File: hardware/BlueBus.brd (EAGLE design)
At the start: 90 x 55 mm, 77 parts, among them J1 USB, Y1 32.768kHz

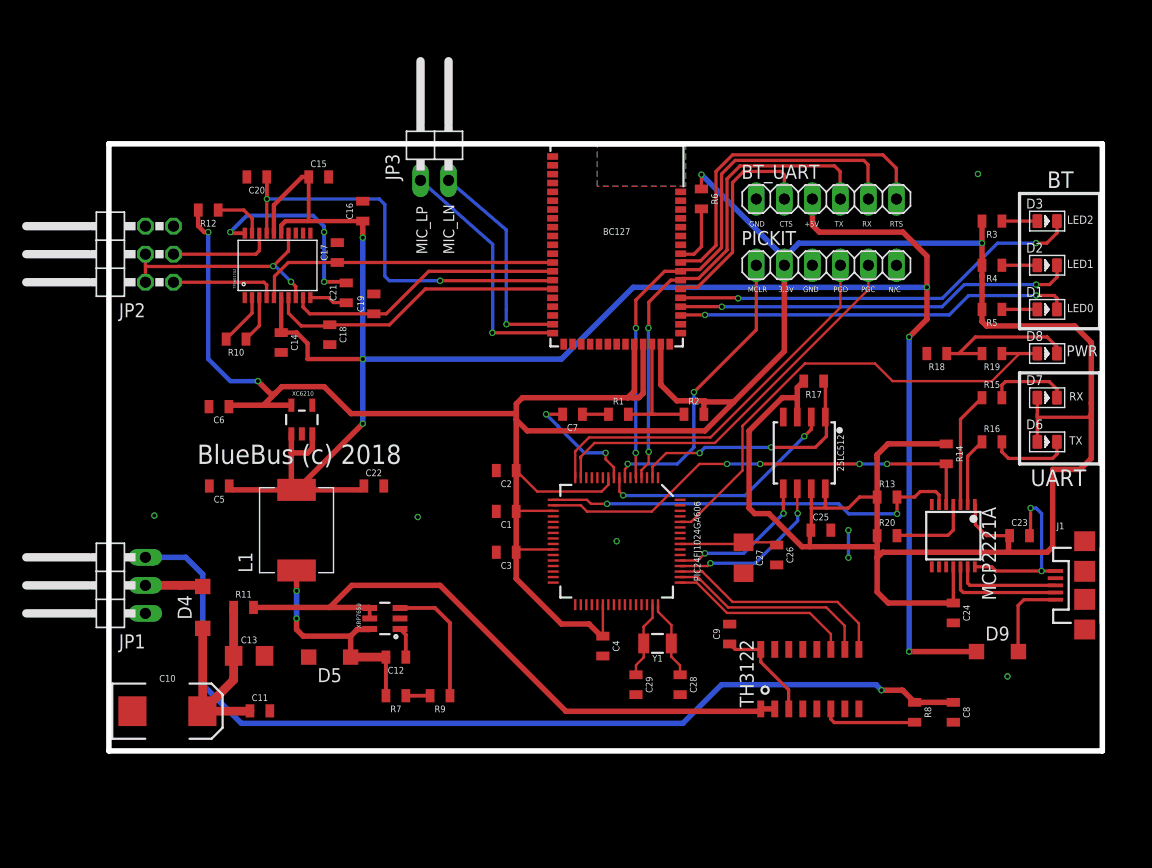
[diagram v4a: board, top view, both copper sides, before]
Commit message: [ADD] hardware: BlueBus v4 Board Changes * Remove BC127 LEDs * Enlarge all IC pads to make SMD assembly easier * Rewire 3.3v Rail into a star topology to do away with potential issues from dasiy chaining * Rewire portions of the 5V rail * Rewire MIC_IN Signals to make use of stereo audio * Tighten up similar signals for better board routing * Enlarge all vias to 0.51mm * Elarge 5v rail to 0.55mm * Tent all vias for a nicer silkscreen * Update silkscreen positioning * Remove wires from under TPA6013 since it contains a thermal pad
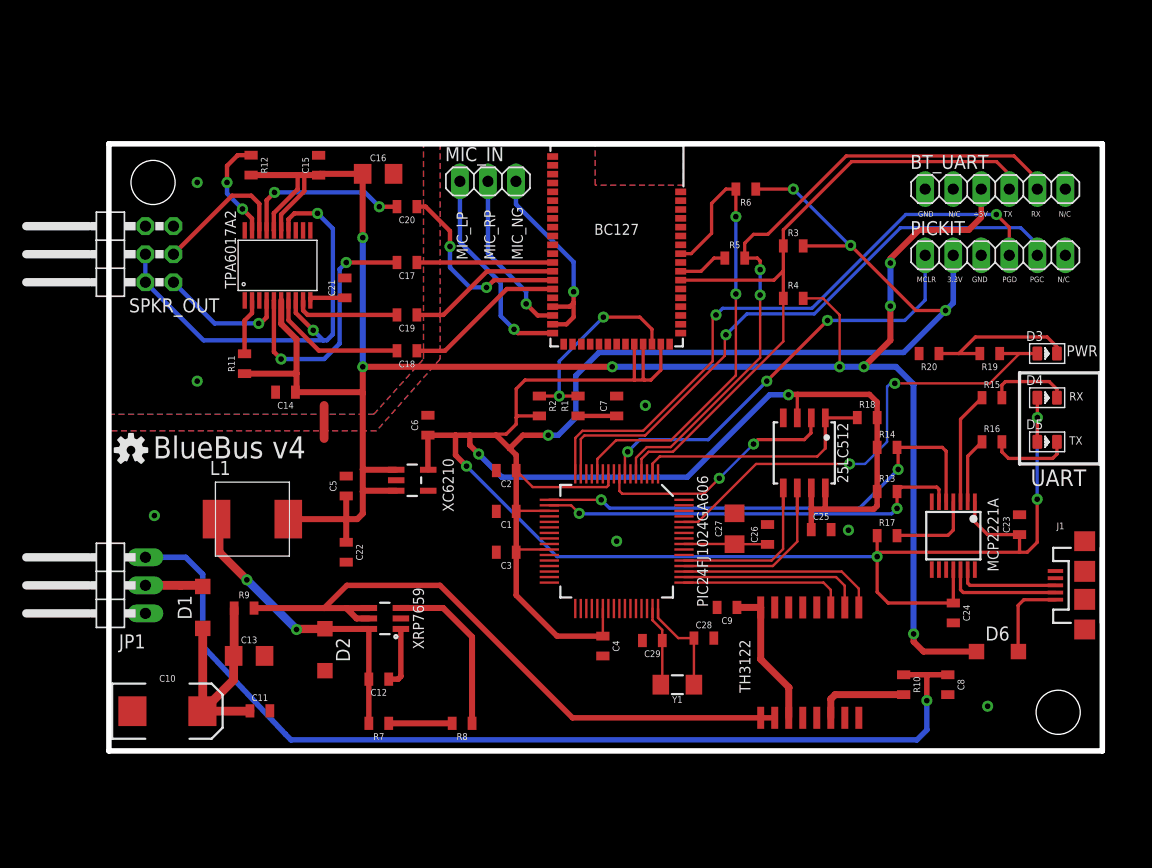
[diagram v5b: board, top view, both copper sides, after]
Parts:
- removed D7, D8: GREEN-0805, Seeed-LED:LED-0805
- removed D9: 2A/30V, Passives:SOD123
- removed JP3: MIC_IN, pinhead:1X02/90
- added MIC_IN: (no value), pinhead:1X03
- added OSHW: (no value), SparkFun-Aesthetics:OSHW-LOGO-S
- BC127: value BC127 -> (none)
- BT_UART: value BT_FTDI -> (none)
- C14, C15: value 0.1uF -> 0.47uF
- C16: value 0.1uF -> 10uF; device Passives:0805 -> Passives:1206
- D1, D6: value RED-0805 -> 2A/30V; device Seeed-LED:LED-0805 -> Passives:SOD123
- D2: value GREEN-0805 -> 2A/30V; device Seeed-LED:LED-0805 -> Passives:SOD123
- D3: value CLEAR-BLUE-0805 -> GREEN-0805
- D4: value 2A/30V -> GREEN-0805; device Passives:SOD123 -> Seeed-LED:LED-0805
- D5: value 2A/30V -> RED-0805; device Passives:SOD123 -> Seeed-LED:LED-0805
- J1: value USB -> (none)
- JP1: value IBUS/VIN -> (none)
- MCP2221A: value MCP2221A -> (none)
- PIC24FJ1024GA606: value PIC24FJ1024GA606 -> (none)
- PICKIT: value MCU_PRGM -> (none)
- R10: value 25k -> 10
- R12: value 10k -> 100k
- R17: value 5.1k -> 10k
- R18: value 2k -> 5.1k
- R20: value 10k -> 2k
- R3, R4, R5: value 240 -> 10k
- R8: value 10 -> 9.09k
- R9: value 9.09k -> 100k
- SPKR_OUT: value SPKR_OUT -> (none)
- TH3122: value TH3122.4SOIC16 -> (none); device TH3122_4:SOIC16 -> TH3122_4:SOIC16DF
- TPA6017A2: value TPA6017A2 -> (none)
- XC6210: value XC6210 -> (none)
- XRP7659: value XRP7659SOT23-6 -> (none)
- Y1: device SparkFun-Clocks:CRYSTAL-SMD-3.2X1.5MM -> Passives:CRYSTAL-SMD-3.2X1.5MM
- moved D1 81.1 mm to (8.50, 13.0), turned to 90 degrees
- moved D4 78.8 mm to (85.0, 32.0), turned to 0 degrees
- moved D2 74.1 mm to (19.6, 9.17), turned to 270 degrees
- moved R10 68.1 mm to (72.0, 6.00), turned to 270 degrees
- moved D5 67.9 mm to (85.0, 28.0), turned to 0 degrees
- moved R8 41.0 mm to (32.0, 2.50), turned to 180 degrees
- moved R5 23.8 mm to (56.7, 44.6), turned to 0 degrees
- moved R11 22.1 mm to (12.3, 35.1), turned to 90 degrees
- moved D6 19.5 mm to (80.5, 9.00)
- moved R9 19.4 mm to (12.2, 12.9), turned to 0 degrees
- moved C6 19.0 mm to (28.9, 29.5), turned to 90 degrees
- moved R4 18.2 mm to (62.0, 41.0), turned to 0 degrees
- moved R3 18.1 mm to (62.0, 45.8), turned to 0 degrees
- moved R20 16.9 mm to (74.3, 36.0), turned to 180 degrees
- moved R17 15.5 mm to (70.5, 19.5), turned to 0 degrees
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- renumbered JP2 to SPKR_OUT
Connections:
- net BT_VBAT_2 renamed VBAT_CAP
- net BYPASS renamed BYP
- removed net BT_UCTS: BC127.40, BT_UART.2
- removed net BT_URTS: BC127.43, BT_UART.6
- removed net GAIN1: R10.1, TPA6017A2.3
- removed net LED0: BC127.37, D1.-
- removed net LED0_RES: D1.+, R5.1
- removed net LED1: BC127.38, D2.-
- removed net LED1_RES: D2.+, R4.1
- removed net LED2: BC127.39, D3.-
- removed net LED2_RES: D3.+, R3.1
- removed net MIC_LN: BC127.20, JP3.2
- new net MIC_NEG: BC127.18, BC127.20, MIC_IN.3
- new net MIC_RP: BC127.19, MIC_IN.2
- net 3.3V: now also D4.+, D5.+, R17.1, R18.2; no longer D6.+, D7.+, R12.2, R17.2, R20.1, R4.2, R5.2
- net 5V: now also D6.C, R11.1, R12.2, R4.2; no longer D9.C
- net BT_RESET: now also PIC24FJ1024GA606.12
- net BT_URX: now also R5.1, R5.2
- net BT_UTX: now also R3.1, R4.1
- net EE_CS: now also R18.1; no longer R17.1
- net FB: now also R8.1; no longer R9.1
- net FB_RES: now also R8.2; no longer R9.2
- net GAIN0: now also R11.2; no longer R10.2
- net GND: now also D2.A, R20.2, TPA6017A2.3; no longer C17.2, C18.2, C19.2, C20.2, D5.A, R18.2
- net IBUS: now also R10.1; no longer R8.1
- net IBUS_IN: now also R10.2; no longer R8.2
- net MCP_5V: now also D6.A; no longer D9.A
- net MCP_LED0_RES: now also D5.-; no longer D6.-
- net MCP_LED1_RES: now also D4.-; no longer D7.-
- net MCP_RESET: now also R17.2; no longer R20.2
- net MIC_LP: now also MIC_IN.1; no longer JP3.1
- net ON_LED: now also D3.+; no longer D8.+
- net ON_LED_RES: now also D3.-, R20.1; no longer D8.-, R18.1
- net SPKR_IN_LN: now also C17.2
- net SPKR_IN_LP: now also C19.2
- net SPKR_IN_RN: now also C20.2
- net SPKR_IN_RP: now also C18.2
- net SW: now also D2.C; no longer D5.C
- net SYS_URX: now also PIC24FJ1024GA606.17; no longer PIC24FJ1024GA606.18
- net SYS_UTX: now also PIC24FJ1024GA606.18; no longer PIC24FJ1024GA606.17
- net VIN: now also D1.A, D1.C, R9.1, R9.2; no longer D4.A, D4.C, R11.1, R11.2
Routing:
- net GND: track 47.7 -> 3.00 mm, vias 14 -> 7
- net LED2: track 37.9 -> 0.00 mm, vias 2 -> 0
- net BT_RESET: track 5.61 -> 42.9 mm, vias 0 -> 2
- net LED1: track 36.3 -> 0.00 mm, vias 2 -> 0
- net LED0: track 36.0 -> 0.00 mm, vias 2 -> 0
- net BT_URTS: track 30.8 -> 0.00 mm
- net MCU_PGD: track 35.6 -> 56.3 mm, vias 0 -> 2
- net SPKR_OUT_NEG: track 21.7 -> 42.0 mm
- net 3.3V: track 344.6 -> 324.7 mm, vias 4 -> 10
- net BT_UCTS: track 19.8 -> 0.00 mm
- net MIC_LN: track 19.6 -> 0.00 mm, vias 1 -> 0
- net MIC_NEG: track 0.00 -> 18.7 mm, vias 0 -> 1
- net MCU_PGC: track 36.6 -> 55.1 mm, vias 0 -> 1
- net BT_UTX: track 45.2 -> 63.2 mm, vias 2 -> 0
- net MIC_RP: track 0.00 -> 15.4 mm, vias 0 -> 1
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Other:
- board text added: "BlueBus v4"
- board text added: "MIC_NG"
- board text added: "MIC_RP"
- board text removed: "BT"
- board text removed: "BlueBus (c) 2018"
- board text removed: "CTS"
- board text removed: "LED0"
- board text removed: "LED1"
- board text removed: "LED2"
- board text removed: "MIC_LN"
- board text removed: "RTS"

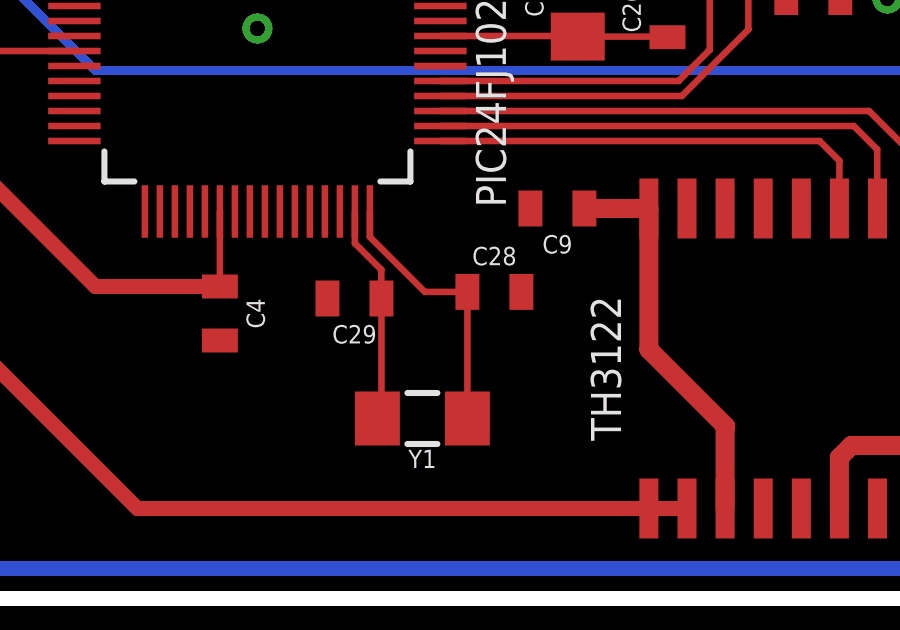
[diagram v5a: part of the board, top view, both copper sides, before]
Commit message: [IMP] hardware: Align crystal caps on the Y-axis
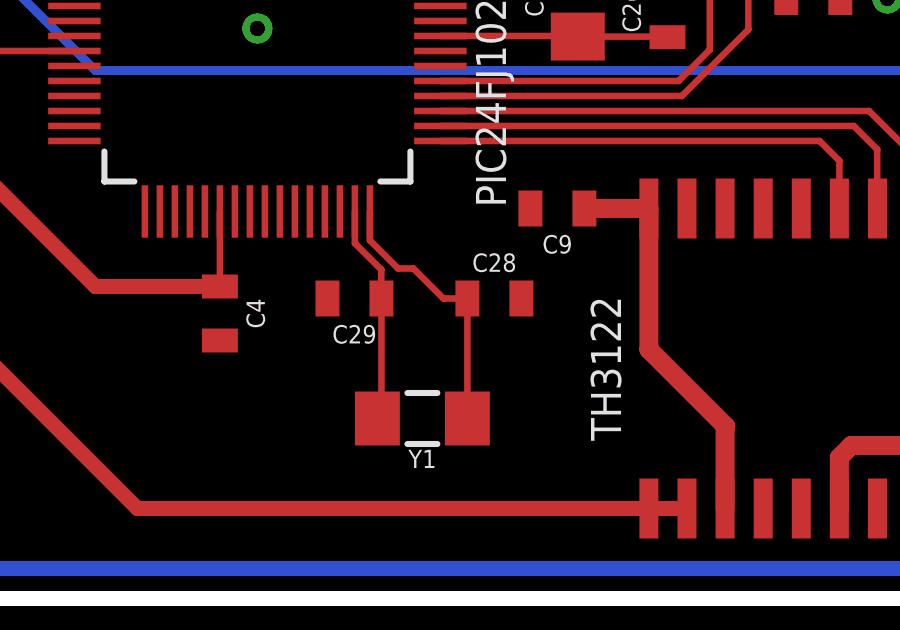
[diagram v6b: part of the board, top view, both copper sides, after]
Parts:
- moved C28 0.22 mm to (53.9, 10.0)
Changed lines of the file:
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@@
 <attribute name="VALUE" x="57.823" y="20.13" size="0.6096" layer="27" font="vector" ratio="20" rot="R90" align="top-center"/>
 </element>
-<element name="C28" library="Passives" package="0805" value="18pF" x="53.9" y="10.22">
-<attribute name="DEVICE" value="18PF-0805-250V" x="53.9" y="10.22" size="1.778" layer="27" display="off"/>
-<attribute name="MFG" value="KEMET" x="53.9" y="10.22" size="1.778" layer="27" display="off"/>
-<attribute name="NAME" x="53.9" y="11.109" size="0.6096" layer="25" font="vector" ratio="20" align="bottom-center"/>
-<attribute name="PACKAGE" value="0805" x="53.9" y="10.22" size="1.778" layer="27" display="off"/>
-<attribute name="PN" value="C0805C180J1GACTU" x="53.9" y="10.22" size="1.778" layer="27" display="off"/>
-<attribute name="VALUE" x="53.9" y="9.331" size="0.6096" layer="27" font="vector" ratio="20" align="top-center"/>
+<element name="C28" library="Passives" package="0805" value="18pF" x="53.9" y="10">
+<attribute name="DEVICE" value="18PF-0805-250V" x="53.9" y="10" size="1.778" layer="27" display="off"/>
+<attribute name="MFG" value="KEMET" x="53.9" y="10" size="1.778" layer="27" display="off"/>
+<attribute name="NAME" x="53.9" y="10.889" size="0.6096" layer="25" font="vector" ratio="20" align="bottom-center"/>
+<attribute name="PACKAGE" value="0805" x="53.9" y="10" size="1.778" layer="27" display="off"/>
+<attribute name="PN" value="C0805C180J1GACTU" x="53.9" y="10" size="1.778" layer="27" display="off"/>
+<attribute name="VALUE" x="53.9" y="9.111" size="0.6096" layer="27" font="vector" ratio="20" align="top-center"/>
 </element>
 <element name="C29" library="Passives" package="0805" value="18pF" x="49.235" y="10" rot="R180">
@@
 <contactref element="C28" pad="1"/>
 <contactref element="Y1" pad="P$1"/>
-<wire x1="49.75" y1="12.9" x2="49.75" y2="12.05" width="0.22" layer="1"/>
-<wire x1="51.58" y1="10.22" x2="53" y2="10.22" width="0.22" layer="1"/>
-<wire x1="49.75" y1="12.05" x2="51.58" y2="10.22" width="0.22" layer="1"/>
-<wire x1="53" y1="10.22" x2="53" y2="6" width="0.22" layer="1"/>
+<wire x1="49.75" y1="12.9" x2="49.75" y2="11.9385" width="0.22" layer="1"/>
+<wire x1="51.2" y1="11" x2="50.6885" y2="11" width="0.22" layer="1"/>
+<wire x1="52.2" y1="10" x2="51.2" y2="11" width="0.22" layer="1"/>
+<wire x1="52.2" y1="10" x2="53" y2="10" width="0.22" layer="1"/>
+<wire x1="49.75" y1="11.9385" x2="50.6885" y2="11" width="0.22" layer="1"/>
+<wire x1="53" y1="10" x2="53" y2="6" width="0.22" layer="1"/>
 </signal>
 <signal name="ON_LED_RES">

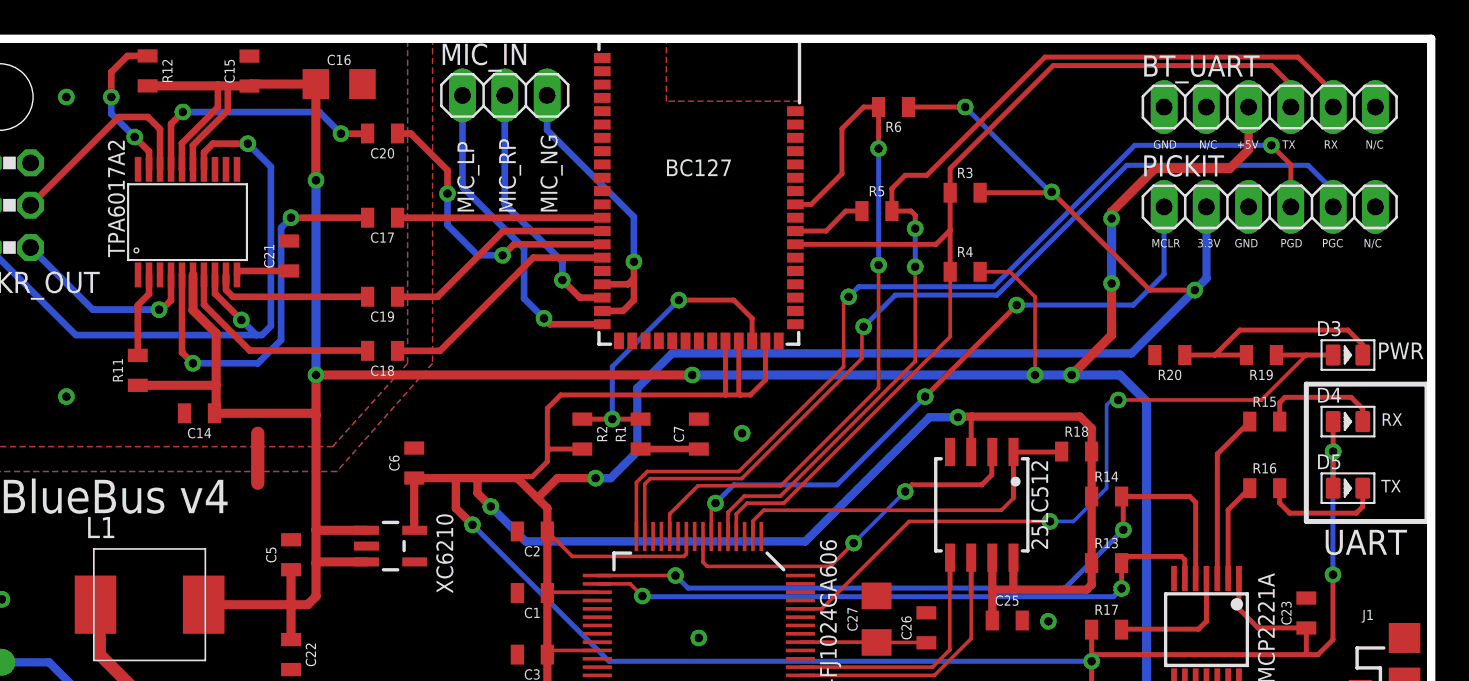
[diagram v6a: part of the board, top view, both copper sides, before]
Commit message: [ADD] hardware: Minor board changes * Add mounting holes * Fix uneven pitch of crystal caps * Replace wide through-hole pins with standard sized ones * Update name of TPA6017A2 IC * Update trace widths for 5v rail to .55mm
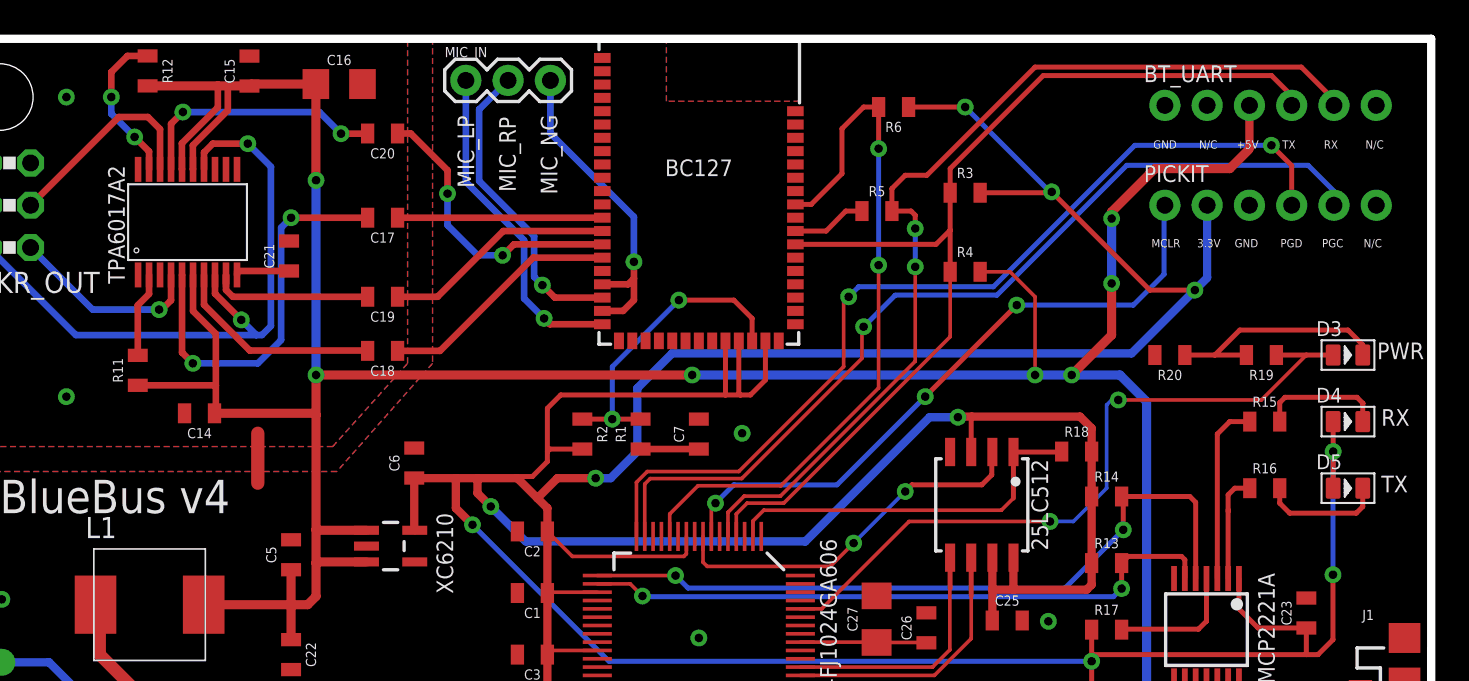
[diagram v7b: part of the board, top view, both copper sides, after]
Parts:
- BT_UART, PICKIT: device pinhead:1X06 -> SparkFun-Connectors:1X06_NO_SILK
- MIC_IN: device pinhead:1X03 -> SparkFun-Connectors:1X03
- moved BT_UART 6.30 mm to (74.0, 51.0)
- moved PICKIT 6.30 mm to (74.0, 45.0)
- moved MIC_IN 2.51 mm to (32.0, 52.5)
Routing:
- net MIC_RP: track 15.4 -> 18.5 mm
- net BT_UTX: track 63.2 -> 62.3 mm
- net MIC_NEG: track 18.7 -> 19.5 mm
- net MIC_LP: track 19.1 -> 19.9 mm
- net BT_URX: track 64.2 -> 63.4 mm
- net MCP_LED1: track 10.2 -> 10.9 mm
- net MCP_LED0: track 5.96 -> 6.49 mm
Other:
- board text removed: "UART"
